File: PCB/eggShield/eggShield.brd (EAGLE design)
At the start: 47.5 x 53.3 mm, 34 parts, among them U1 V_REG_LDOSMD, U2 V_REG_LDOSMD

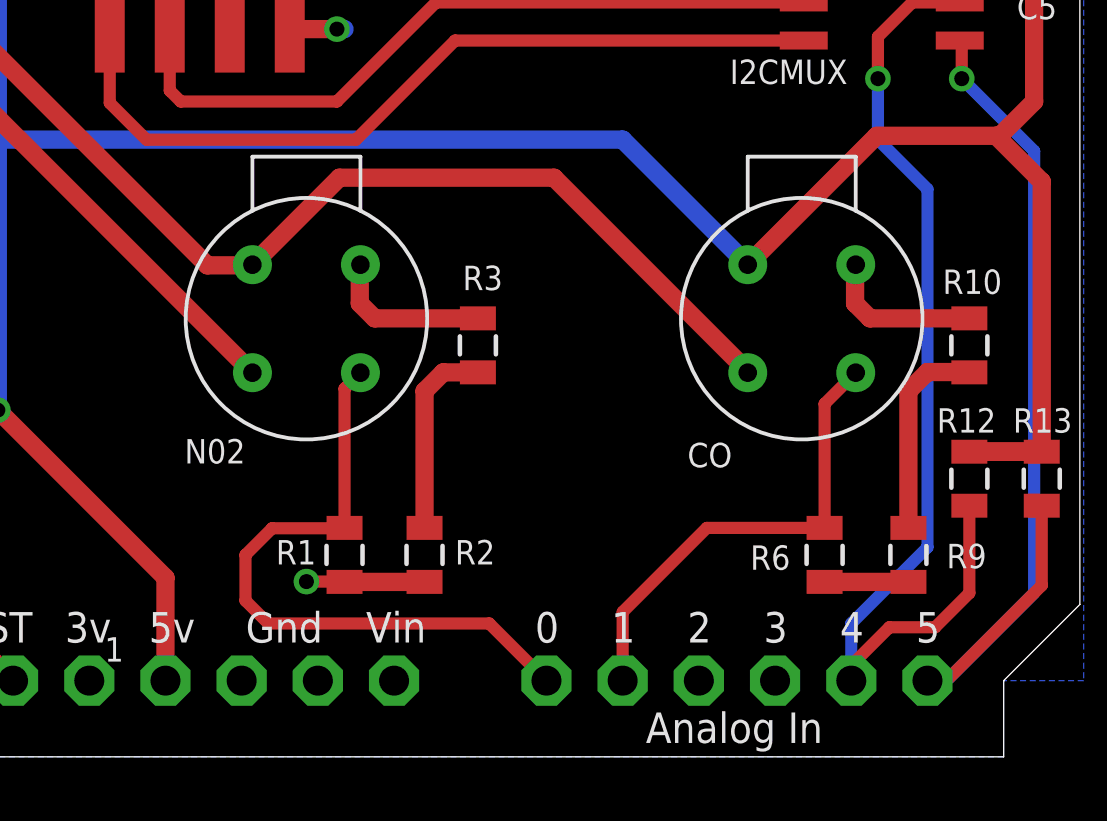
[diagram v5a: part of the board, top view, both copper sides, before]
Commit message: added routing for range select signals to arduino header and updated silkscreen for e2v sensors
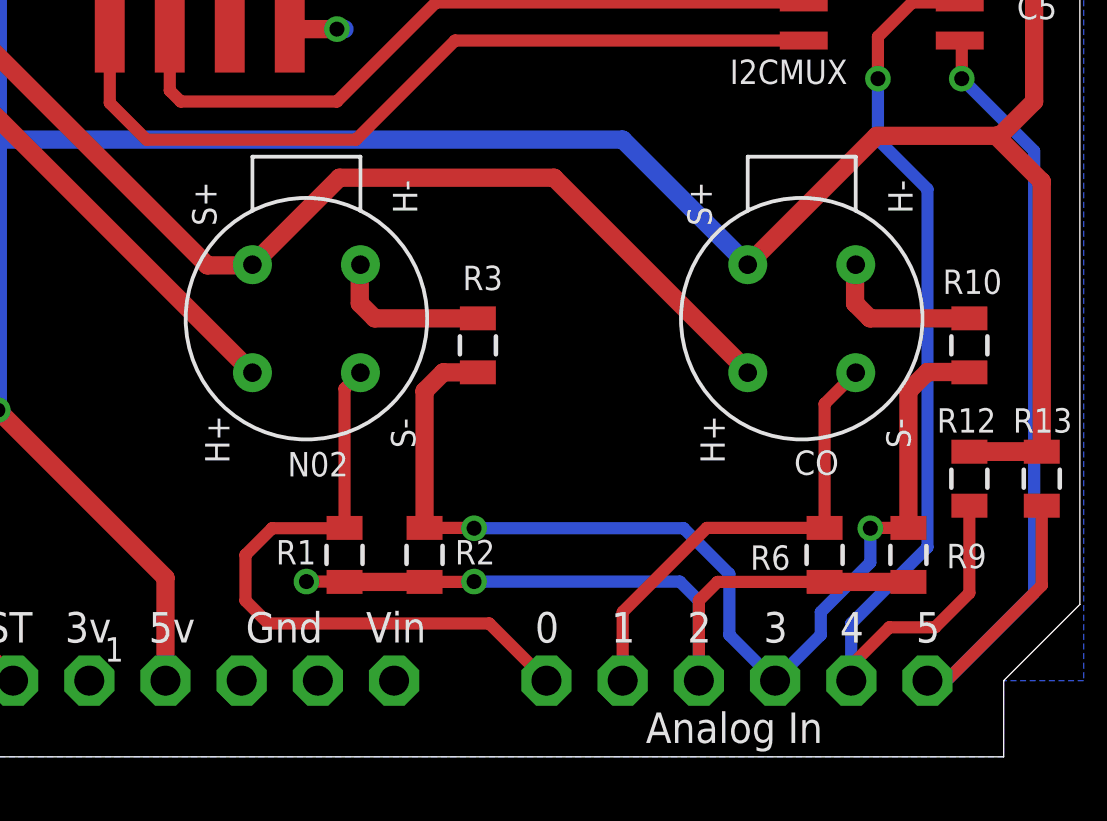
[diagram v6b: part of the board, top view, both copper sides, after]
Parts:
- R4, R7: value 150Ohm -> 2.4MOhm
- R5: value 330Ohm -> 1MOhm
- R8: value 330Ohm -> 2.4MOhm
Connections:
- net 2.5V renamed 2.4V
- removed net /CO_R1_SEL: R6.1, R9.2
- removed net /CO_R2_SEL: R10.2, R9.1
- removed net /NO2_R1_SEL: R1.1, R2.2
- removed net /NO2_R2_SEL: R2.1, R3.2
- new net /SENSE_R1_SEL: R1.1, R2.2, R6.1, R9.2, U$7.A2
- new net /SENSE_R2_SEL: R10.2, R2.1, R3.2, R9.1, U$7.A3
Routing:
- net /SENSE_R2_SEL: track 0.00 -> 36.1 mm, vias 0 -> 2
- net /SENSE_R1_SEL: track 0.00 -> 25.9 mm, vias 0 -> 2
- net /CO_R2_SEL: track 6.86 -> 0.00 mm
- net /NO2_R2_SEL: track 6.60 -> 0.00 mm
- net /NO2_R1_SEL: track 3.94 -> 0.00 mm, vias 1 -> 0
- net /CO_R1_SEL: track 2.79 -> 0.00 mm
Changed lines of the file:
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@@
 </element>
 <element name="N02" library="ricardo" package="SR-4" value="E2V" x="21.717" y="14.605" smashed="yes" rot="R90">
-<attribute name="NAME" x="17.653" y="9.779" size="0.8128" layer="25" font="vector"/>
+<attribute name="NAME" x="23.114" y="10.16" size="0.8128" layer="25" font="vector" rot="R180"/>
 </element>
 <element name="R1" library="SparkFun" package="0805" value="" x="22.987" y="6.731" smashed="yes" rot="R90">
@@
 <attribute name="VALUE" x="24.384" y="5.715" size="0.4064" layer="27" rot="R90"/>
 </element>
-<element name="R4" library="SparkFun" package="0805" value="150Ohm" x="4.064" y="14.986" smashed="yes">
+<element name="R4" library="SparkFun" package="0805" value="2.4MOhm" x="4.064" y="14.986" smashed="yes">
 <attribute name="NAME" x="1.27" y="14.6685" size="0.8128" layer="25" font="vector"/>
 <attribute name="VALUE" x="3.048" y="13.589" size="0.4064" layer="27"/>
 </element>
-<element name="R5" library="SparkFun" package="0805" value="330Ohm" x="7.493" y="14.986" smashed="yes">
+<element name="R5" library="SparkFun" package="0805" value="1MOhm" x="7.493" y="14.986" smashed="yes">
 <attribute name="NAME" x="9.144" y="14.6685" size="0.8128" layer="25" font="vector"/>
 <attribute name="VALUE" x="6.477" y="13.589" size="0.4064" layer="27"/>
@@
 <attribute name="VALUE" x="2.203" y="35.011" size="0.3048" layer="27" rot="R90"/>
 </element>
-<element name="R7" library="SparkFun" package="0805" value="150Ohm" x="4.064" y="27.813" smashed="yes">
+<element name="R7" library="SparkFun" package="0805" value="2.4MOhm" x="4.064" y="27.813" smashed="yes">
 <attribute name="NAME" x="1.27" y="27.4955" size="0.8128" layer="25" font="vector"/>
 <attribute name="VALUE" x="3.048" y="26.416" size="0.4064" layer="27"/>
 </element>
-<element name="R8" library="SparkFun" package="0805" value="330Ohm" x="7.493" y="27.813" smashed="yes">
+<element name="R8" library="SparkFun" package="0805" value="2.4MOhm" x="7.493" y="27.813" smashed="yes">
 <attribute name="NAME" x="9.271" y="27.4955" size="0.8128" layer="25" font="vector"/>
 <attribute name="VALUE" x="6.477" y="26.416" size="0.4064" layer="27"/>
@@
 </element>
 <element name="CO" library="ricardo" package="SR-4" value="E2V" x="38.227" y="14.605" smashed="yes" rot="R90">
-<attribute name="NAME" x="34.417" y="9.652" size="0.8128" layer="25" font="vector"/>
+<attribute name="NAME" x="37.973" y="9.398" size="0.8128" layer="25" font="vector"/>
 </element>
 <element name="R6" library="SparkFun" package="0805" value="" x="38.989" y="6.731" smashed="yes" rot="R90">
@@
 <wire x1="19.177" y1="44.323" x2="19.685" y2="44.323" width="0.6096" layer="16"/>
 </signal>
-<signal name="/NO2_R1_SEL">
-<contactref element="R1" pad="1"/>
-<contactref element="R2" pad="2"/>
-<wire x1="22.987" y1="5.831" x2="25.654" y2="5.831" width="0.6096" layer="1"/>
-<via x="21.717" y="5.842" extent="1-16" drill="0.5"/>
-<wire x1="21.717" y1="5.842" x2="22.976" y2="5.842" width="0.4064" layer="1"/>
-<wire x1="22.976" y1="5.842" x2="22.987" y2="5.831" width="0.4064" layer="1"/>
-</signal>
-<signal name="/NO2_R2_SEL">
-<contactref element="R2" pad="1"/>
-<contactref element="R3" pad="2"/>
-<wire x1="25.654" y1="7.631" x2="25.654" y2="12.192" width="0.6096" layer="1"/>
-<wire x1="27.432" y1="12.816" x2="26.278" y2="12.816" width="0.6096" layer="1"/>
-<wire x1="26.278" y1="12.816" x2="25.654" y2="12.192" width="0.6096" layer="1"/>
-</signal>
 <signal name="N$1">
 <contactref element="R5" pad="1"/>
@@
 <wire x1="8.763" y1="21.204" x2="8.321" y2="20.762" width="0.6096" layer="1"/>
 </signal>
-<signal name="2.5V">
+<signal name="2.4V">
 <contactref element="C9" pad="P$1"/>
 <contactref element="R8" pad="2"/>
@@
 <wire x1="10.16" y1="35.814" x2="8.763" y2="37.211" width="0.6096" layer="1"/>
 </signal>
-<signal name="/CO_R1_SEL">
+<signal name="/SENSE_R1_SEL">
 <contactref element="R6" pad="1"/>
 <contactref element="R9" pad="2"/>
 <wire x1="38.989" y1="5.831" x2="41.783" y2="5.831" width="0.6096" layer="1"/>
-</signal>
-<signal name="/CO_R2_SEL">
+<contactref element="R1" pad="1"/>
+<contactref element="R2" pad="2"/>
+<wire x1="22.987" y1="5.831" x2="25.654" y2="5.831" width="0.6096" layer="1"/>
+<via x="21.717" y="5.842" extent="1-16" drill="0.5"/>
+<wire x1="21.717" y1="5.842" x2="22.976" y2="5.842" width="0.4064" layer="1"/>
+<wire x1="22.976" y1="5.842" x2="22.987" y2="5.831" width="0.4064" layer="1"/>
+<contactref element="U$7" pad="A2"/>
+<wire x1="38.989" y1="5.831" x2="35.422" y2="5.831" width="0.4064" layer="1"/>
+<wire x1="35.422" y1="5.831" x2="34.798" y2="5.207" width="0.4064" layer="1"/>
+<wire x1="34.798" y1="5.207" x2="34.798" y2="2.54" width="0.4064" layer="1"/>
+<wire x1="25.654" y1="5.831" x2="27.294" y2="5.831" width="0.4064" layer="1"/>
+<wire x1="27.294" y1="5.831" x2="27.305" y2="5.842" width="0.4064" layer="1"/>
+<via x="27.305" y="5.842" extent="1-16" drill="0.5"/>
+<wire x1="27.305" y1="5.842" x2="34.163" y2="5.842" width="0.4064" layer="16"/>
+<wire x1="34.163" y1="5.842" x2="34.798" y2="5.207" width="0.4064" layer="16"/>
+<wire x1="34.798" y1="5.207" x2="34.798" y2="2.54" width="0.4064" layer="16"/>
+</signal>
+<signal name="/SENSE_R2_SEL">
 <contactref element="R9" pad="1"/>
 <contactref element="R10" pad="2"/>
@@
 <wire x1="42.418" y1="12.827" x2="43.804" y2="12.827" width="0.6096" layer="1"/>
 <wire x1="43.804" y1="12.827" x2="43.815" y2="12.816" width="0.6096" layer="1"/>
+<contactref element="R2" pad="1"/>
+<contactref element="R3" pad="2"/>
+<wire x1="25.654" y1="7.631" x2="25.654" y2="12.192" width="0.6096" layer="1"/>
+<wire x1="27.432" y1="12.816" x2="26.278" y2="12.816" width="0.6096" layer="1"/>
+<wire x1="26.278" y1="12.816" x2="25.654" y2="12.192" width="0.6096" layer="1"/>
+<contactref element="U$7" pad="A3"/>
+<wire x1="41.783" y1="7.631" x2="40.524" y2="7.631" width="0.4064" layer="1"/>
+<wire x1="40.524" y1="7.631" x2="40.513" y2="7.62" width="0.4064" layer="1"/>
+<via x="40.513" y="7.62" extent="1-16" drill="0.5"/>
+<wire x1="25.654" y1="7.631" x2="27.294" y2="7.631" width="0.4064" layer="1"/>
+<wire x1="27.294" y1="7.631" x2="27.305" y2="7.62" width="0.4064" layer="1"/>
+<via x="27.305" y="7.62" extent="1-16" drill="0.5"/>
+<wire x1="27.305" y1="7.62" x2="34.29" y2="7.62" width="0.4064" layer="16"/>
+<wire x1="34.29" y1="7.62" x2="35.814" y2="6.096" width="0.4064" layer="16"/>
+<wire x1="35.814" y1="6.096" x2="35.814" y2="4.064" width="0.4064" layer="16"/>
+<wire x1="35.814" y1="4.064" x2="37.338" y2="2.54" width="0.4064" layer="16"/>
+<wire x1="40.513" y1="7.62" x2="40.513" y2="6.477" width="0.4064" layer="16"/>
+<wire x1="40.513" y1="6.477" x2="38.862" y2="4.826" width="0.4064" layer="16"/>
+<wire x1="38.862" y1="4.826" x2="38.862" y2="4.064" width="0.4064" layer="16"/>
+<wire x1="38.862" y1="4.064" x2="37.338" y2="2.54" width="0.4064" layer="16"/>
 </signal>
 <signal name="D3">

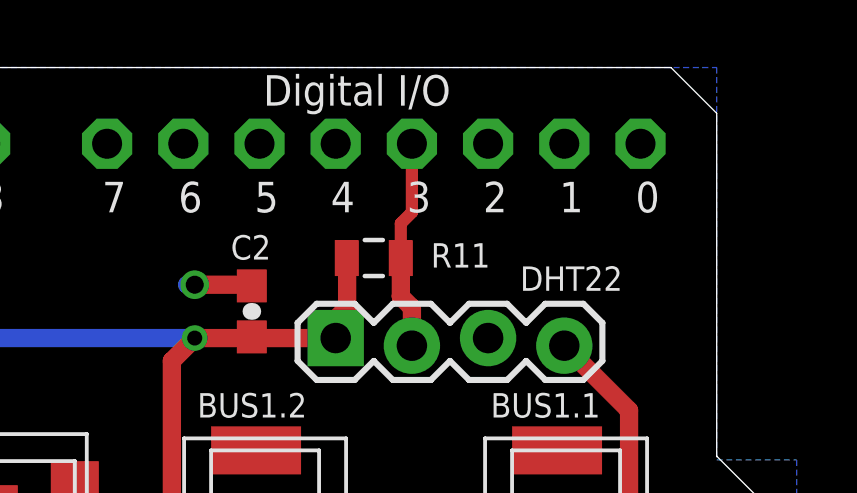
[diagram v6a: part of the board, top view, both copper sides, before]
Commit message: changed DHT22 I/O to DIG2, changed LDO feedback resistor values again,  added more documentation to the schematic
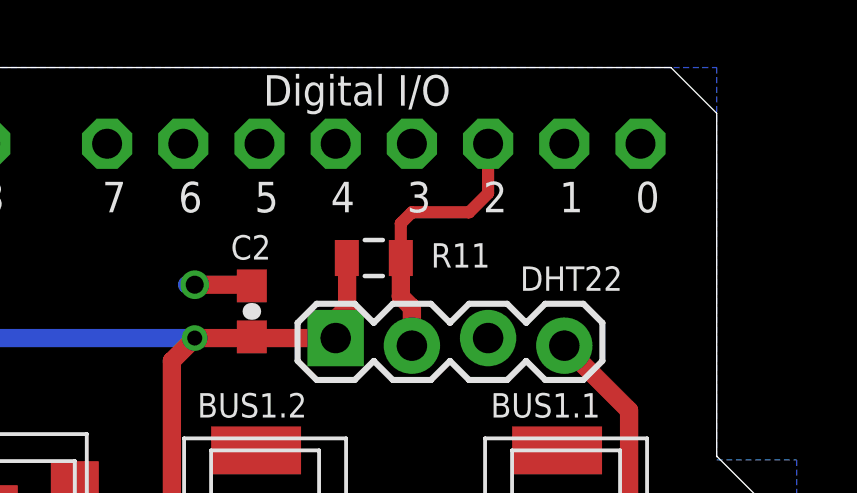
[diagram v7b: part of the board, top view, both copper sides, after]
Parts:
- R4: value 2.4MOhm -> 1.8MOhm
- R5: value 1MOhm -> 750kOhm
- R7, R8: value 2.4MOhm -> 750kOhm
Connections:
- removed net D3: DHT22.DATA, R11.2, U$7.D3
- new net DHT22_IO: DHT22.DATA, R11.2, U$7.D2
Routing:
- net DHT22_IO: track 0.00 -> 9.21 mm
- net D3: track 7.04 -> 0.00 mm
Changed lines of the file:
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@@
 <attribute name="VALUE" x="24.384" y="5.715" size="0.4064" layer="27" rot="R90"/>
 </element>
-<element name="R4" library="SparkFun" package="0805" value="2.4MOhm" x="4.064" y="14.986" smashed="yes">
+<element name="R4" library="SparkFun" package="0805" value="1.8MOhm" x="4.064" y="14.986" smashed="yes">
 <attribute name="NAME" x="1.27" y="14.6685" size="0.8128" layer="25" font="vector"/>
 <attribute name="VALUE" x="3.048" y="13.589" size="0.4064" layer="27"/>
 </element>
-<element name="R5" library="SparkFun" package="0805" value="1MOhm" x="7.493" y="14.986" smashed="yes">
+<element name="R5" library="SparkFun" package="0805" value="750kOhm" x="7.493" y="14.986" smashed="yes">
 <attribute name="NAME" x="9.144" y="14.6685" size="0.8128" layer="25" font="vector"/>
 <attribute name="VALUE" x="6.477" y="13.589" size="0.4064" layer="27"/>
@@
 <attribute name="VALUE" x="2.203" y="35.011" size="0.3048" layer="27" rot="R90"/>
 </element>
-<element name="R7" library="SparkFun" package="0805" value="2.4MOhm" x="4.064" y="27.813" smashed="yes">
+<element name="R7" library="SparkFun" package="0805" value="750kOhm" x="4.064" y="27.813" smashed="yes">
 <attribute name="NAME" x="1.27" y="27.4955" size="0.8128" layer="25" font="vector"/>
 <attribute name="VALUE" x="3.048" y="26.416" size="0.4064" layer="27"/>
 </element>
-<element name="R8" library="SparkFun" package="0805" value="2.4MOhm" x="7.493" y="27.813" smashed="yes">
+<element name="R8" library="SparkFun" package="0805" value="750kOhm" x="7.493" y="27.813" smashed="yes">
 <attribute name="NAME" x="9.271" y="27.4955" size="0.8128" layer="25" font="vector"/>
 <attribute name="VALUE" x="6.477" y="26.416" size="0.4064" layer="27"/>
@@
 <wire x1="38.862" y1="4.064" x2="37.338" y2="2.54" width="0.4064" layer="16"/>
 </signal>
-<signal name="D3">
-<contactref element="DHT22" pad="DATA"/>
-<contactref element="U$7" pad="D3"/>
-<contactref element="R11" pad="2"/>
-<wire x1="34.428" y1="46.99" x2="34.428" y2="45.709" width="0.6096" layer="1"/>
-<wire x1="34.428" y1="45.709" x2="34.798" y2="45.339" width="0.6096" layer="1"/>
-<wire x1="34.798" y1="45.339" x2="34.798" y2="44.069" width="0.6096" layer="1"/>
-<wire x1="34.428" y1="46.99" x2="34.428" y2="48.144" width="0.4064" layer="1"/>
-<wire x1="34.428" y1="48.144" x2="34.798" y2="48.514" width="0.4064" layer="1"/>
-<wire x1="34.798" y1="48.514" x2="34.798" y2="50.8" width="0.4064" layer="1"/>
-</signal>
 <signal name="3V">
 <contactref element="U$7" pad="3V"/>
@@
 <wire x1="17.161" y1="22.209" x2="17.526" y2="21.844" width="0.4064" layer="1"/>
 </signal>
+<signal name="DHT22_IO">
+<contactref element="U$7" pad="D2"/>
+<contactref element="DHT22" pad="DATA"/>
+<contactref element="R11" pad="2"/>
+<wire x1="34.428" y1="46.99" x2="34.428" y2="45.709" width="0.6096" layer="1"/>
+<wire x1="34.428" y1="45.709" x2="34.798" y2="45.339" width="0.6096" layer="1"/>
+<wire x1="34.798" y1="45.339" x2="34.798" y2="44.069" width="0.6096" layer="1"/>
+<wire x1="34.428" y1="46.99" x2="34.428" y2="48.144" width="0.4064" layer="1"/>
+<wire x1="34.428" y1="48.144" x2="34.798" y2="48.514" width="0.4064" layer="1"/>
+<wire x1="34.798" y1="48.514" x2="36.703" y2="48.514" width="0.4064" layer="1"/>
+<wire x1="36.703" y1="48.514" x2="37.338" y2="49.149" width="0.4064" layer="1"/>
+<wire x1="37.338" y1="49.149" x2="37.338" y2="50.8" width="0.4064" layer="1"/>
+</signal>
 </signals>

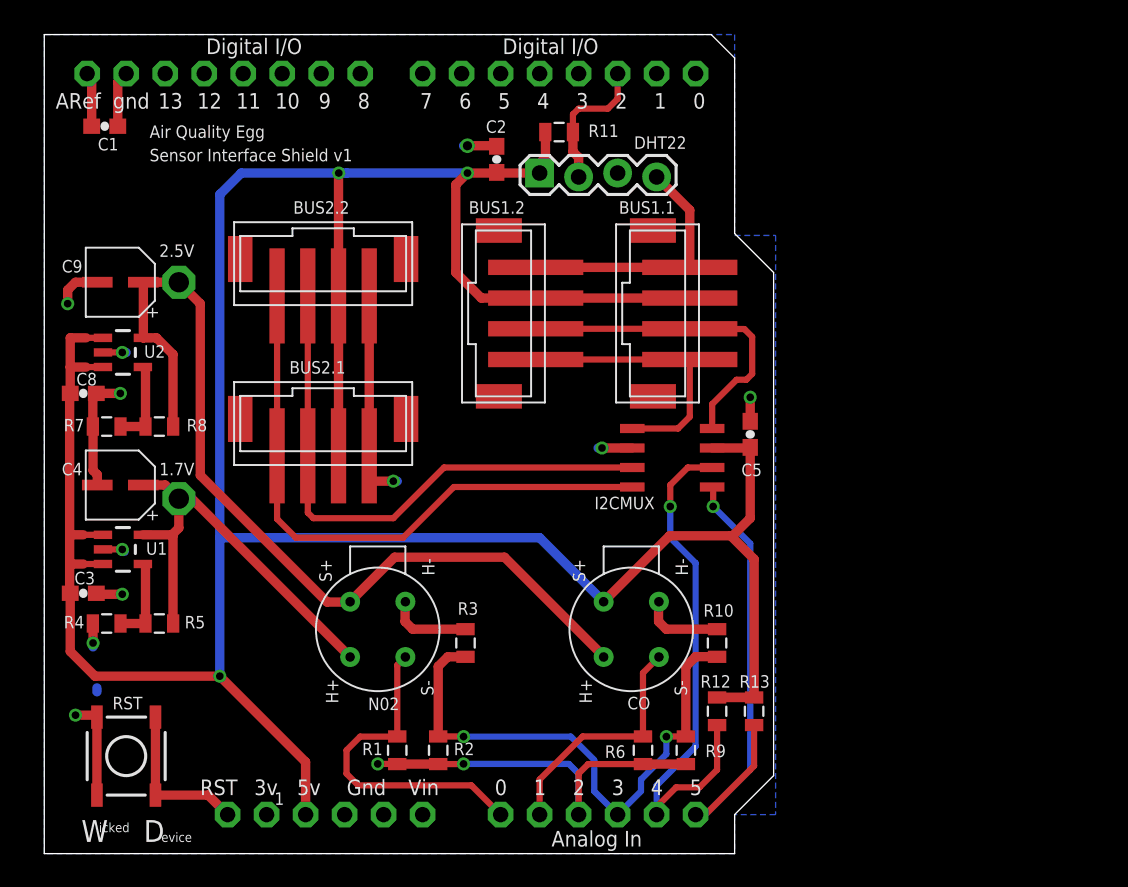
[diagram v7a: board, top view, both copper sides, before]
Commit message: added registration holes
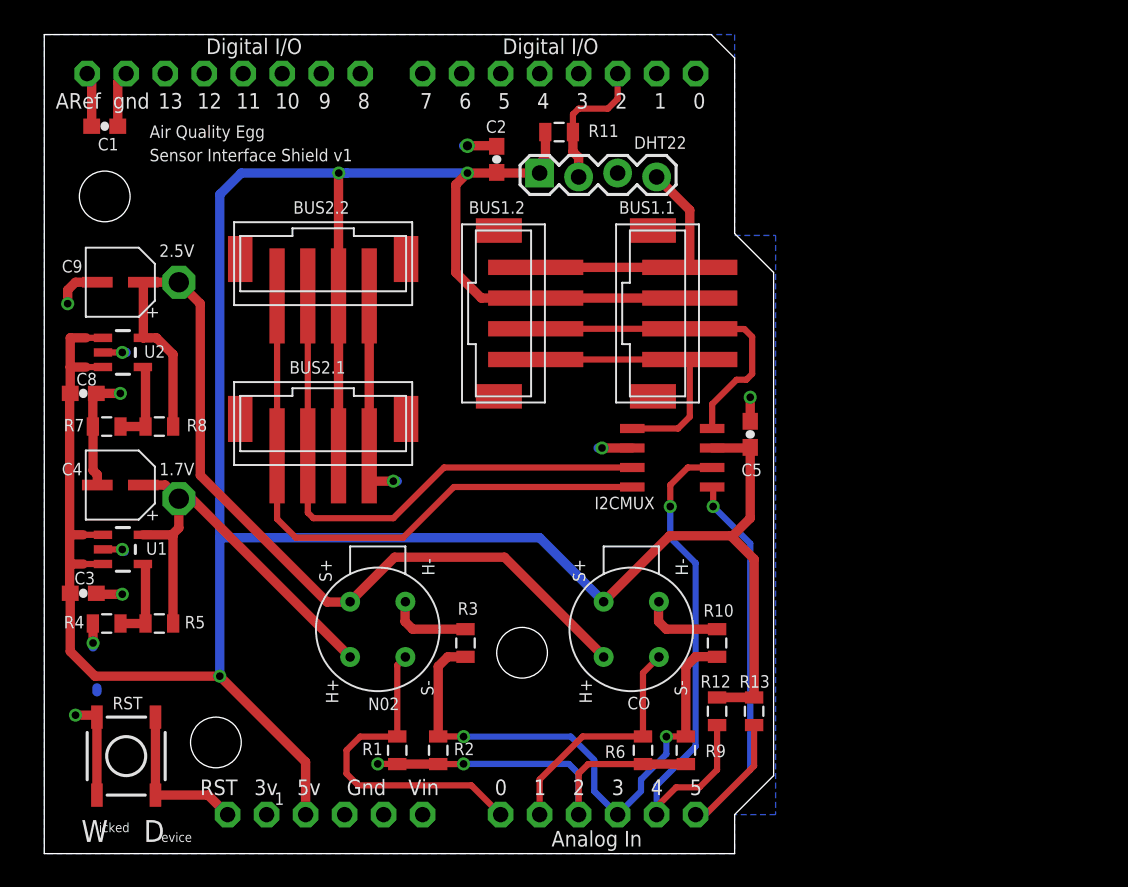
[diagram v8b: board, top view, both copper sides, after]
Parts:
- added JP1, JP2, JP3: STAND-OFF, SparkFun:STAND-OFF
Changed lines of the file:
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@@
 <attribute name="NAME" x="19.616" y="32.073" size="0.8128" layer="25" font="vector" rot="R180"/>
 </element>
+<element name="JP1" library="SparkFun" package="STAND-OFF" value="STAND-OFF" x="31.115" y="13.081"/>
+<element name="JP2" library="SparkFun" package="STAND-OFF" value="STAND-OFF" x="3.937" y="42.799"/>
+<element name="JP3" library="SparkFun" package="STAND-OFF" value="STAND-OFF" x="11.176" y="7.239" rot="MR0"/>
 </elements>
 <signals>
